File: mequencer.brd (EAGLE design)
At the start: 102.5 x 80 mm, 69 parts, among them IC1 NE555D, IC10 LF353D, IC11 NE555D, IC12 NE555D, IC2 4163D, IC3 74HC85D, IC4 4051D, IC5 4051D, IC6 74HCT04D, IC7 4051D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

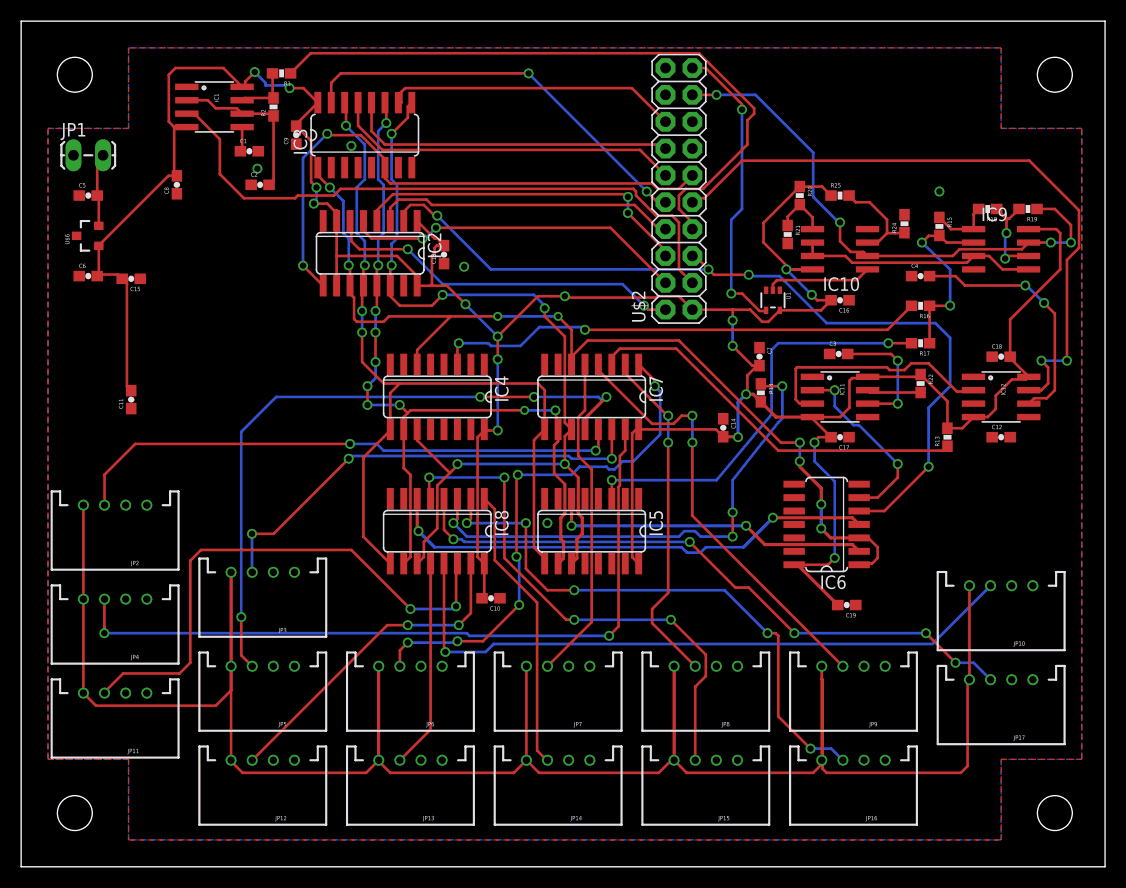
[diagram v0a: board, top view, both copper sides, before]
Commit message: test points and jack resistors
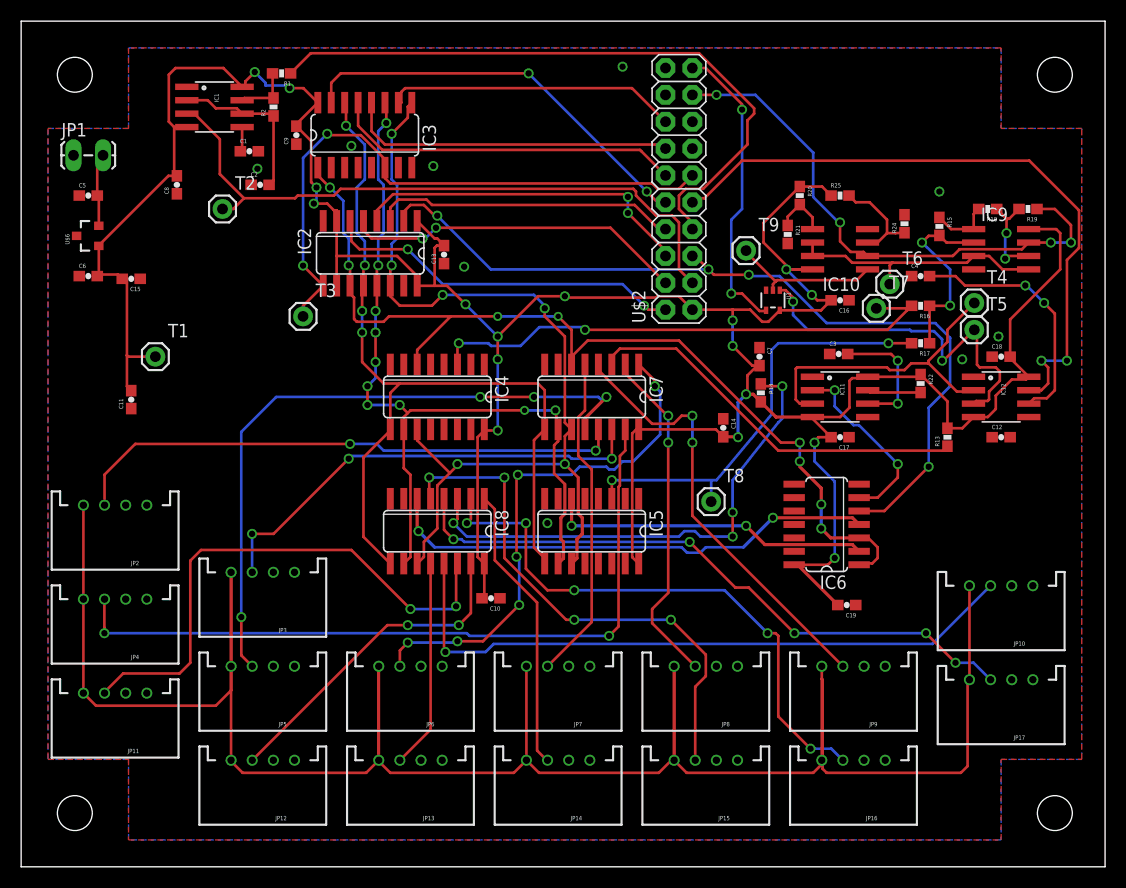
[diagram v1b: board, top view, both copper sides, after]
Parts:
- added T1, T2, T3, T4, T5, T6, T7, T8, T9: M01PTH, SparkFun-Connectors:1X01
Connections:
- removed net VSS: IC2.8
- net 5V: now also C12.2, T1.1
- net CHANNEL0: now also JP2.2
- net CHANNEL10: now also JP12.2
- net CHANNEL11: now also JP13.2
- net CHANNEL12: now also JP14.2
- net CHANNEL13: now also JP15.2
- net CHANNEL14: now also JP16.2
- net CHANNEL15: now also JP17.2
- net CHANNEL2: now also JP4.2
- net CHANNEL3: now also JP5.2
- net CHANNEL4: now also JP6.2
- net CHANNEL5: now also JP7.2
- net CHANNEL6: now also JP8.2
- net CHANNEL7: now also JP9.2
- net CHANNEL8: now also JP10.2
- net CHANNEL9: now also JP11.2
- net GND: now also IC2.8
- net HIGH_OUT: now also T8.1
- net INT_CLOCK: now also T2.1
- net LOAD: now also T3.1
- net LOW_OUT: now also T7.1
- net N$22: now also T9.1
- net N$23: now also T4.1
- net N$25: now also IC12.3, T5.1
- net VGND: now also T6.1
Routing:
- net N$25: track 0.00 -> 35.1 mm, vias 0 -> 2
- net N$23: track 23.0 -> 30.6 mm
- net N$22: track 10.1 -> 14.2 mm
- net LOAD: track 54.4 -> 58.1 mm
- net LOW_OUT: track 46.8 -> 49.8 mm
- net 5V: track 308.4 -> 310.9 mm
- net INT_CLOCK: track 60.0 -> 62.4 mm
- net VGND: track 22.8 -> 24.9 mm
- net HIGH_OUT: track 39.4 -> 41.4 mm
